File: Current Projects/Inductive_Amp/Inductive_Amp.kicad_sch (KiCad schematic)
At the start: 10 parts, among them J1 Conn_01x03, J2 Conn_01x03, U1 NA555D, U2 74LS14, U3 TLV2372

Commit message: Inductive PCB!
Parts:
- added C3, C6, C7, C8, C9: 0.1u, Capacitor_SMD:C_0805_2012Metric, symbol Device:C
- added C4, C5: 1u, Capacitor_SMD:C_0805_2012Metric, symbol Device:C
- added D1, D2: PESD5V0S2BT, Package_TO_SOT_SMD:SOT-23-3, symbol Custom_Power_Protection:PESD5V0S2BT
- added H1, H2, H3, H4: M2, MountingHole:MountingHole_2.2mm_M2_DIN965_Pad, symbol Mechanical:MountingHole_Pad
- added R4, R5: 1k, Resistor_SMD:R_0805_2012Metric, symbol Device:R
- added unit 6 of U2
- added unit 4 of U2
- added unit 5 of U2
- added unit 3 of U2
- added unit 3 of U3
- added unit 2 of U3
- J1: value Conn_01x03 -> INPUT
- J2: value Conn_01x03 -> OUTPUT
- R2: value 1k -> 15k
- R3: value 200 -> 10k
- U2: footprint Package_SO:SOIC-14_3.9x8.7mm_P1.27mm -> (none)
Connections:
- net +5V: now also U2.3, C3.1, C4.1, C5.1, C6.1, C7.1, C8.1, C9.1, D1.2, D2.1, U2.11, U2.13, U2.5, U2.9, U3.8 (V+)
- net GND: now also C3.2, C4.2, C5.2, C6.2, C7.2, C8.2, C9.2, D1.3, D2.3, U3.4 (V-), U3.5 (+)
- net OUT: now also D2.2, R5.2; no longer U1.3 (Q)
- net Vin: now also D1.1, R4.1; no longer U3.3 (+)
- net at R2.2, U3.1: now also U2.1; no longer U2.3
- net at U2.4: no longer U2.1
- new net: R4.2, U3.3 (+)
- new net: U3.6 (-), U3.7
- new net: R5.1, U1.3 (Q)
- no-connect marks 0 -> 9
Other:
- note added: "Gain = 1 + (R2 / R3) 1 + (15k / 10k) = 2.5"
- note added: "Low Pulse (ignore): ~400mV High Pulse (capture): ~1V - 1.2V High P -> AMP -> 1.9V or higher Low P -> AMP -> less than 1.4V Gain = ~2.5 is ideal"
- note added: "VT+: 1.4V - 1.9V"
- moved on the sheet: C1, C2, J1, J2, R1, R2, R3, U1, U2A, U2G

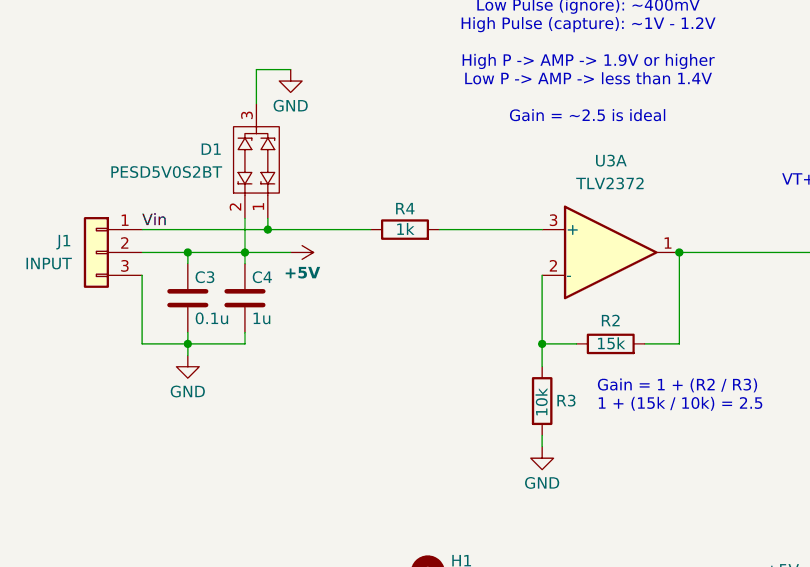
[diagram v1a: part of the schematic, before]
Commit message: Inductive PCB pull down R
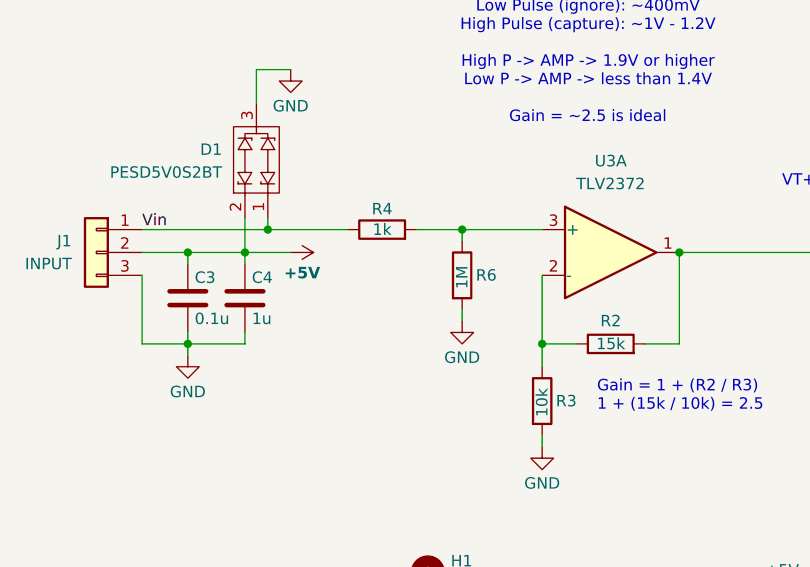
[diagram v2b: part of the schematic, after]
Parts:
- added R6: 1M, Resistor_SMD:R_0805_2012Metric, symbol Device:R
- U2: footprint (none) -> Package_SO:SOIC-14_3.9x8.7mm_P1.27mm
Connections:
- net GND: now also R6.2
- net at R4.2, U3.3 (+): now also R6.1
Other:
- moved on the sheet: R4
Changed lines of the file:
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@@
 	)
 	(junction
+		(at 80.01 80.01)
+		(diameter 0)
+		(color 0 0 0 0)
+	)
+	(junction
 		(at 218.44 85.09)
 		(diameter 0)
@@
 	(wire
 		(pts
+			(xy 80.01 90.17) (xy 80.01 88.9)
+		)
+		(stroke
+			(width 0)
+			(type default)
+		)
+	)
+	(wire
+		(pts
+			(xy 80.01 80.01) (xy 88.9 80.01)
+		)
+		(stroke
+			(width 0)
+			(type default)
+		)
+	)
+	(wire
+		(pts
 			(xy 184.15 118.11) (xy 184.15 116.84)
 		)
@@
 	(wire
 		(pts
+			(xy 80.01 81.28) (xy 80.01 80.01)
+		)
+		(stroke
+			(width 0)
+			(type default)
+		)
+	)
+	(wire
+		(pts
 			(xy 224.79 93.98) (xy 224.79 95.25)
 		)
@@
 	(wire
 		(pts
-			(xy 58.42 80.01) (xy 69.85 80.01)
+			(xy 58.42 80.01) (xy 67.31 80.01)
 		)
 		(stroke
@@
 	(wire
 		(pts
-			(xy 77.47 80.01) (xy 88.9 80.01)
+			(xy 74.93 80.01) (xy 80.01 80.01)
 		)
 		(stroke
@@
 			)
 		)
-		(property "Footprint" ""
+		(property "Footprint" "Package_SO:SOIC-14_3.9x8.7mm_P1.27mm"
 			(at 144.78 62.23 0)
 			(effects
@@
 	)
 	(symbol
+		(lib_id "power:GND")
+		(at 80.01 90.17 0)
+		(unit 1)
+		(exclude_from_sim no)
+		(in_bom yes)
+		(on_board yes)
+		(dnp no)
+		(property "Reference" "#PWR025"
+			(at 80.01 96.52 0)
+			(effects
+				(font
+					(size 1.27 1.27)
+				)
+				(hide yes)
+			)
+		)
+		(property "Value" "GND"
+			(at 80.01 94.234 0)
+			(effects
+				(font
+					(size 1.27 1.27)
+				)
+			)
+		)
+		(property "Footprint" ""
+			(at 80.01 90.17 0)
+			(effects
+				(font
+					(size 1.27 1.27)
+				)
+				(hide yes)
+			)
+		)
+		(property "Datasheet" ""
+			(at 80.01 90.17 0)
+			(effects
+				(font
+					(size 1.27 1.27)
+				)
+				(hide yes)
+			)
+		)
+		(property "Description" "Power symbol creates a global label with name \"GND\" , ground"
+			(at 80.01 90.17 0)
+			(effects
+				(font
+					(size 1.27 1.27)
+				)
+				(hide yes)
+			)
+		)
+		(pin "1"
+		)
+		(instances
+			(project "Inductive_Amp"
+				(path "/98a5ffd3-028c-4fe9-b0d1-6655fc45bd8e"
+					(reference "#PWR025")
+					(unit 1)
+				)
+			)
+		)
+	)
+	(symbol
 		(lib_id "Device:C")
 		(at 49.53 87.63 0)
@@
 	)
 	(symbol
+		(lib_id "Device:R")
+		(at 80.01 85.09 0)
+		(unit 1)
+		(exclude_from_sim no)
+		(in_bom yes)
+		(on_board yes)
+		(dnp no)
+		(property "Reference" "R6"
+			(at 81.534 85.09 0)
+			(effects
+				(font
+					(size 1.27 1.27)
+				)
+				(justify left)
+			)
+		)
+		(property "Value" "1M"
+			(at 80.01 86.614 90)
+			(effects
+				(font
+					(size 1.27 1.27)
+				)
+				(justify left)
+			)
+		)
+		(property "Footprint" "Resistor_SMD:R_0805_2012Metric"
+			(at 78.232 85.09 90)
+			(effects
+				(font
+					(size 1.27 1.27)
+				)
+				(hide yes)
+			)
+		)
+		(property "Datasheet" "~"
+			(at 80.01 85.09 0)
+			(effects
+				(font
+					(size 1.27 1.27)
+				)
+				(hide yes)
+			)
+		)
+		(property "Description" "Resistor"
+			(at 80.01 85.09 0)
+			(effects
+				(font
+					(size 1.27 1.27)
+				)
+				(hide yes)
+			)
+		)
+		(pin "1"
+		)
+		(pin "2"
+		)
+		(instances
+			(project ""
+				(path "/98a5ffd3-028c-4fe9-b0d1-6655fc45bd8e"
+					(reference "R6")
+					(unit 1)
+				)
+			)
+		)
+	)
+	(symbol
 		(lib_id "Device:C")
 		(at 167.64 113.03 0)
@@
 	(symbol
 		(lib_id "Device:R")
-		(at 73.66 80.01 90)
+		(at 71.12 80.01 90)
 		(unit 1)
 		(exclude_from_sim no)
@@
 		(dnp no)
 		(property "Reference" "R4"
-			(at 73.66 77.724 90)
+			(at 71.12 77.724 90)
 			(effects
 				(font
@@
 		)
 		(property "Value" "1k"
-			(at 73.66 80.01 90)
+			(at 71.12 80.01 90)
 			(effects
 				(font
@@
 		)
 		(property "Footprint" "Resistor_SMD:R_0805_2012Metric"
-			(at 73.66 81.788 90)
+			(at 71.12 81.788 90)
 			(effects
 				(font
@@
 		)
 		(property "Datasheet" "~"
-			(at 73.66 80.01 0)
+			(at 71.12 80.01 0)
 			(effects
 				(font
@@
 		)
 		(property "Description" "Resistor"
-			(at 73.66 80.01 0)
+			(at 71.12 80.01 0)
 			(effects
 				(font

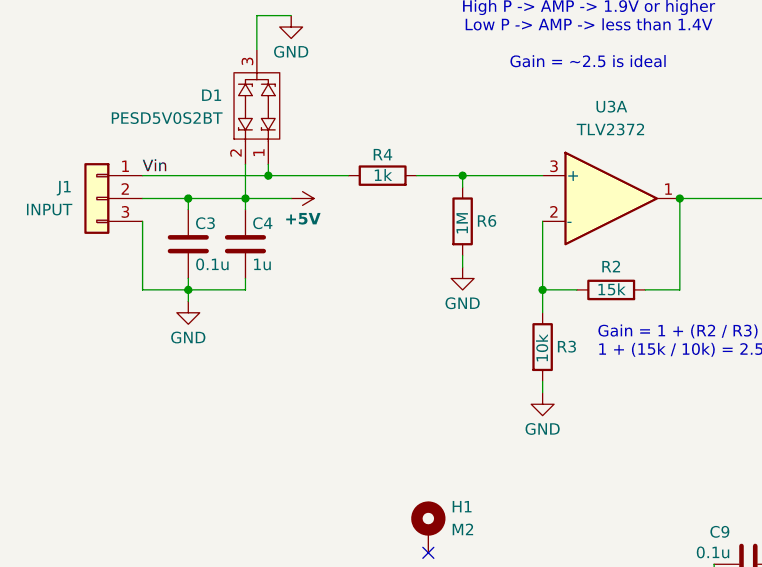
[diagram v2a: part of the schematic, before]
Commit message: Inductive sch annotations and silkscreen name change
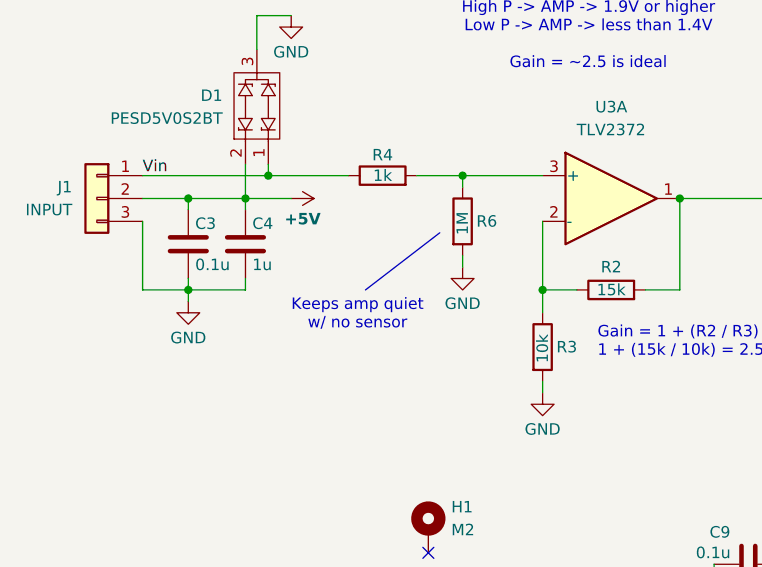
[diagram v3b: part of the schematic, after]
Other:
- note added: "Keeps amp quiet w/ no sensor"
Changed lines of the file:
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@@
+		)
+	)
+	(text "Keeps amp quiet\nw/ no sensor"
+		(exclude_from_sim no)
+		(at 68.326 95.504 0)
+		(effects
+			(font
+				(size 1.27 1.27)
+			)
 		)
 	)
@@
 		)
 		(stroke
+			(width 0)
+			(type default)
+		)
+	)
+	(polyline
+		(pts
+			(xy 69.215 92.71) (xy 77.47 86.36)
+		)
+		(stroke

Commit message: Inductive amp fab files
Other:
- note added: "IC Power Blocks"
- note added: "Terminated Unused Gates"
- moved on the sheet: C1, C2, C3, C4, C5, C6, C7, C8, C9, D1, D2, H1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
